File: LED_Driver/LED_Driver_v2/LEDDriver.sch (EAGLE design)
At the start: 14 parts, among them Q1 DMP2012SN-7, U1 LM3409HV'LM3409HV'

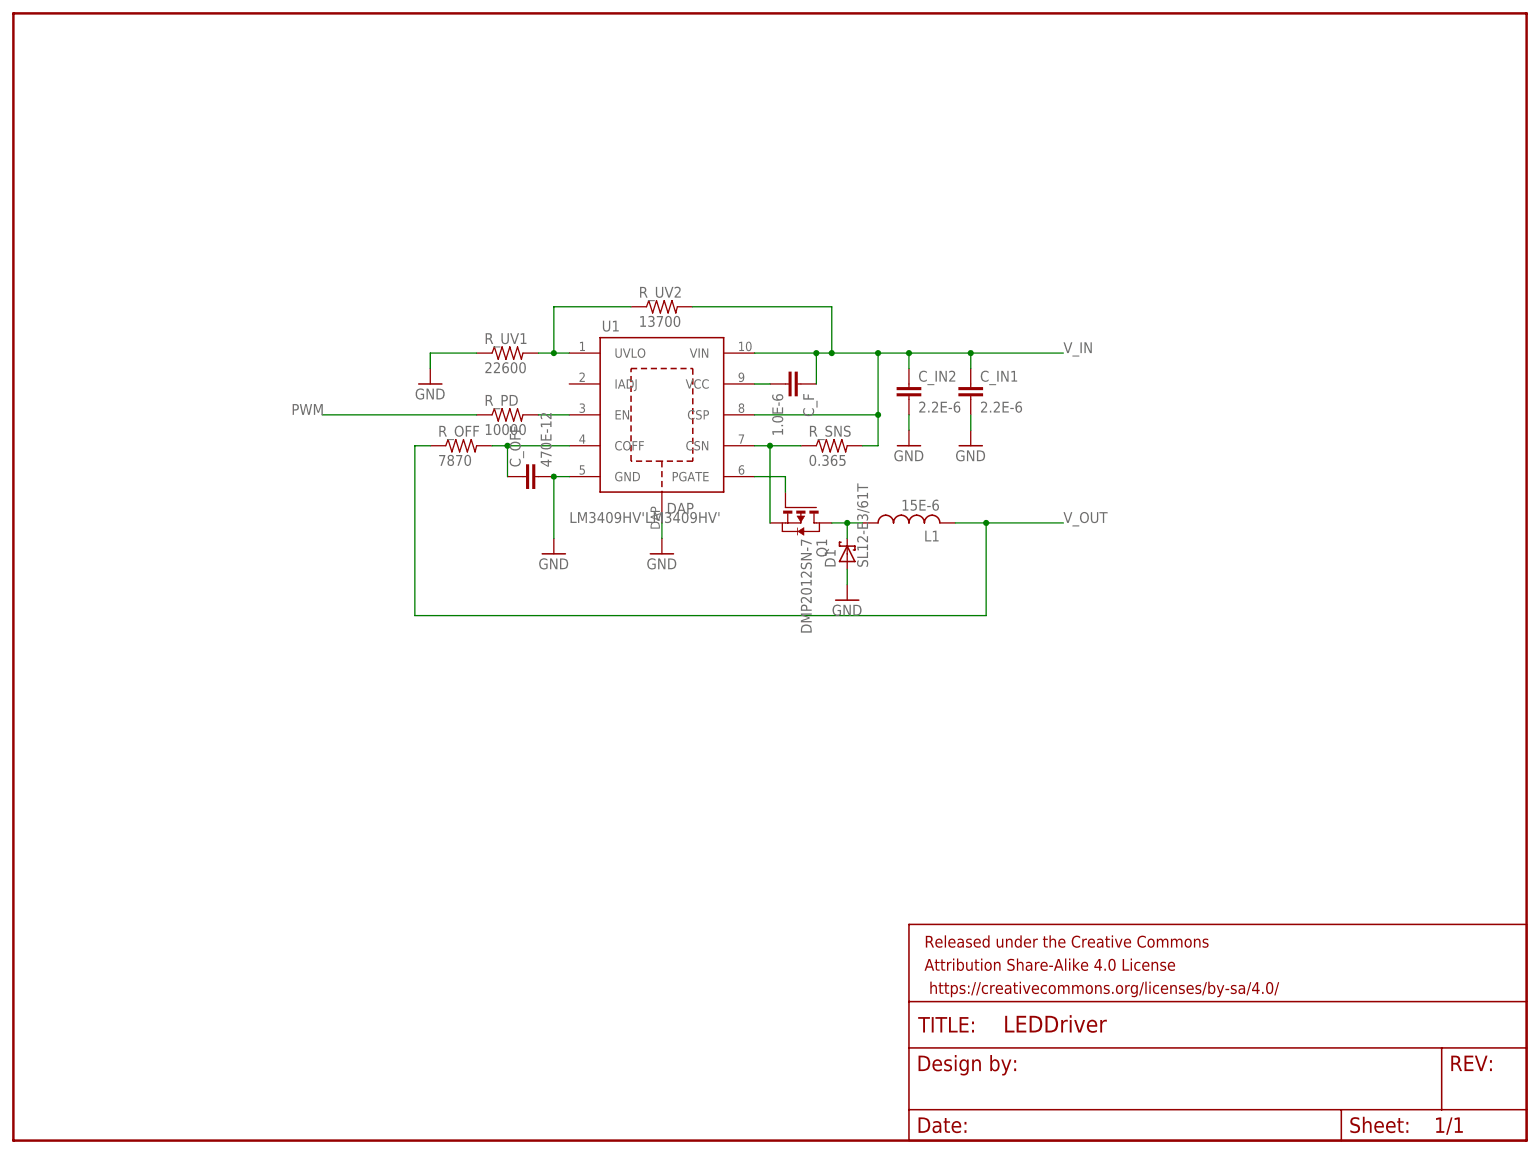
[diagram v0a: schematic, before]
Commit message: Minor changes to trace placement in LED Driver v2
Minor changes to trace placement in LED Driver v2
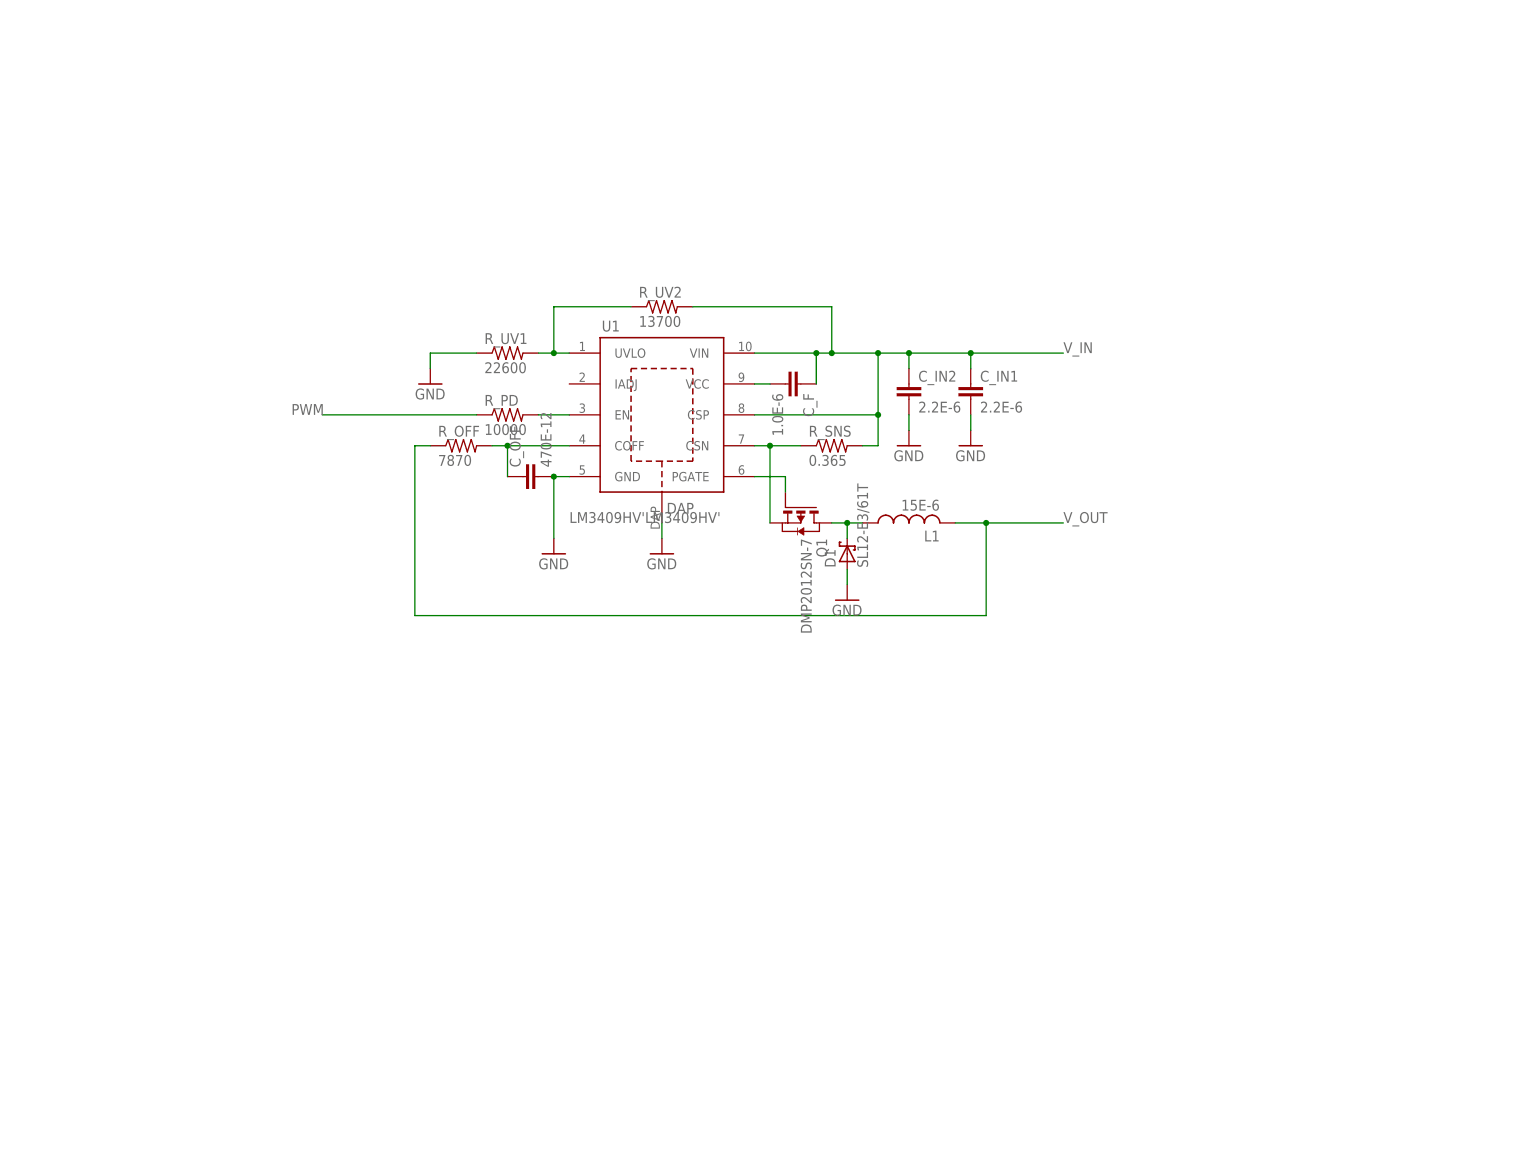
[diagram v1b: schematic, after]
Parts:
- removed FRAME1: FRAME-LETTER, SparkFun-Aesthetics:FRAME-LETTER
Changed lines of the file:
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@@
 </classes>
 <parts>
-<part name="FRAME1" library="SparkFun-Aesthetics" deviceset="FRAME-LETTER" device=""/>
 <part name="R_UV2" library="DiscreteComponents" deviceset="R-US_" device="R0603" value="13700"/>
 <part name="R_UV1" library="DiscreteComponents" deviceset="R-US_" device="R0603" value="22600"/>
@@
 </plain>
 <instances>
-<instance part="FRAME1" gate="G$1" x="0" y="0"/>
-<instance part="FRAME1" gate="V" x="147.32" y="0"/>
 <instance part="R_UV2" gate="G$1" x="106.68" y="137.16"/>
 <instance part="R_UV1" gate="G$1" x="81.28" y="129.54"/>
